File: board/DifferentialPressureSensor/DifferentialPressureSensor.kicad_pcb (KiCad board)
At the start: 2 copper layers, 119.5 x 65 mm, 15 parts, among them U1 ESP32-S3-DEVKIT-LIPO

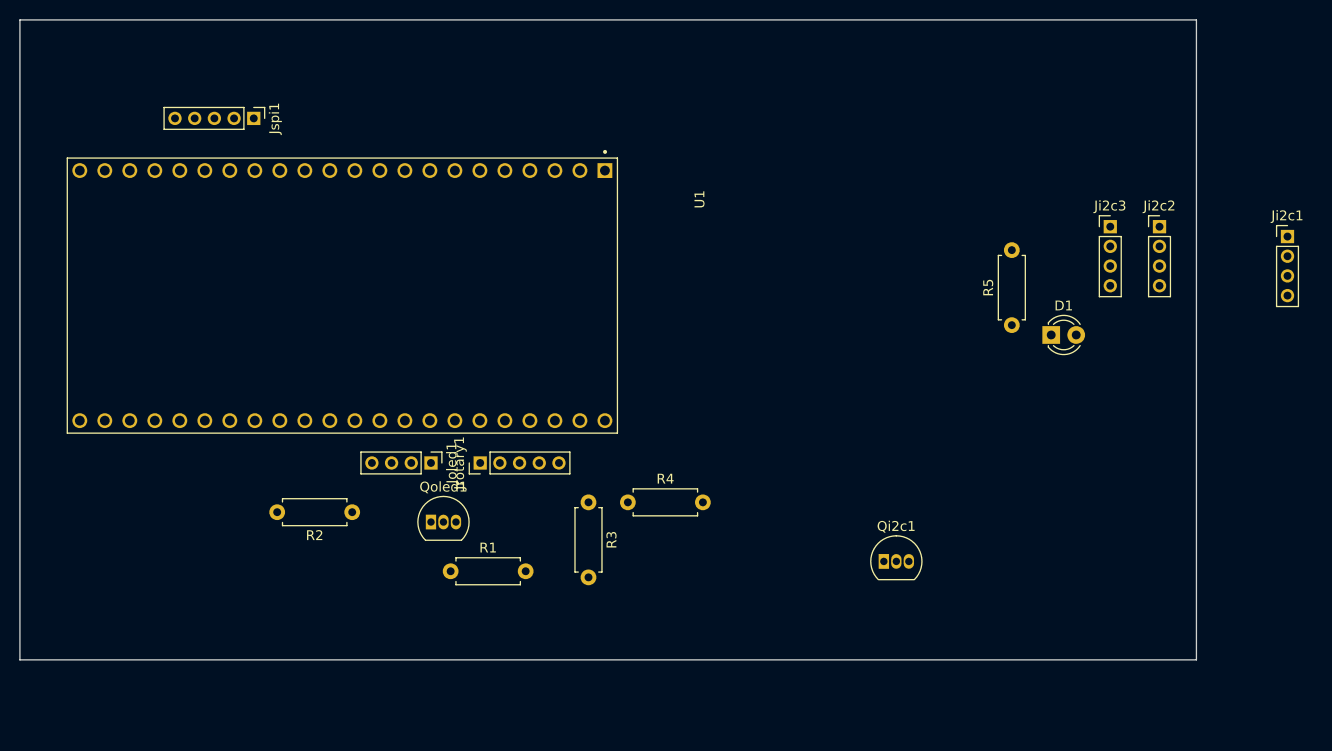
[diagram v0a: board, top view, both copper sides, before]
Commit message: updated pins on sch file and completed routing of PCB, sucks bad, but holds togeter with 1 layer only :-D
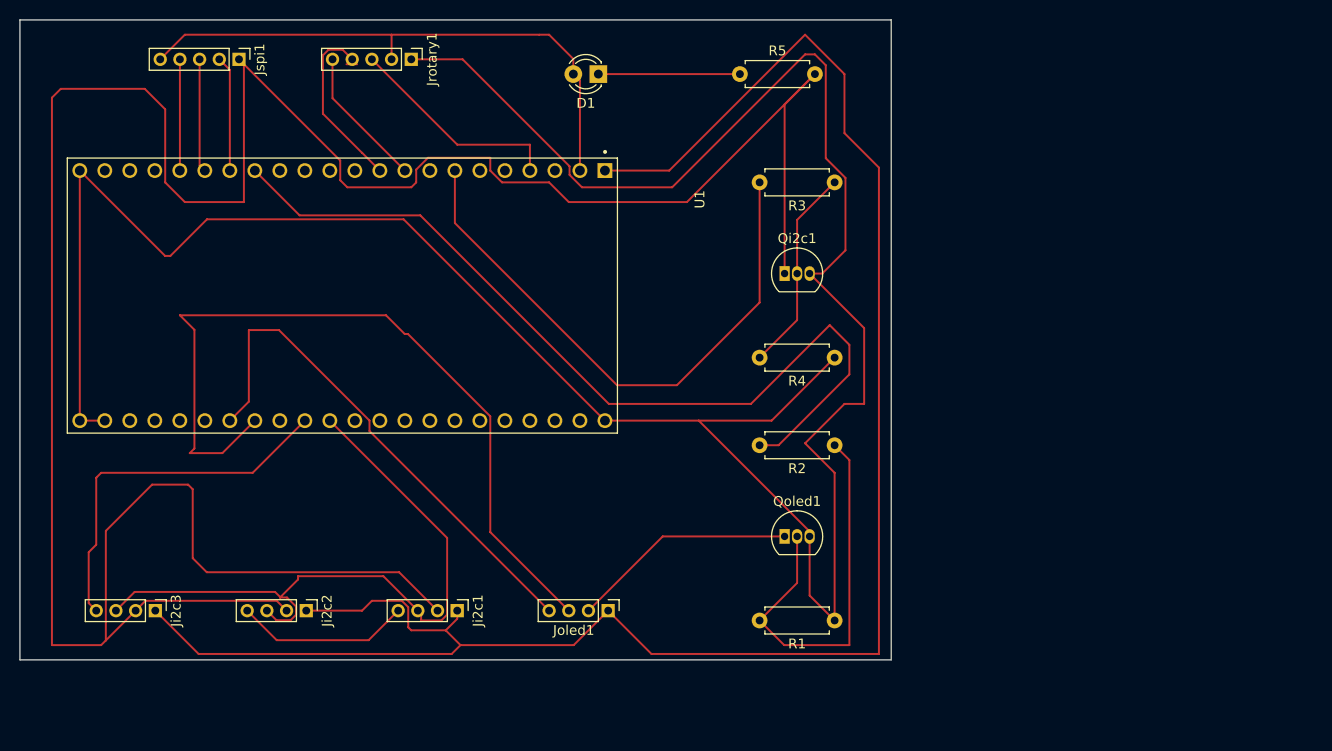
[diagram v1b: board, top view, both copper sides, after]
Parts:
- R4: value 10k -> 4.7k
- R5: value 2k -> 4.7k
- moved Ji2c3 104.5 mm to (27.0, 81.0), turned to -90 degrees
- moved Ji2c2 95.0 mm to (42.3, 81.0), turned to -90 degrees
- moved Ji2c1 92.5 mm to (57.7, 81.0), turned to -90 degrees
- moved D1 53.1 mm to (72.0, 26.5), turned to 180 degrees
- moved R2 49.5 mm to (96.0, 64.2)
- moved Jrotary1 41.6 mm to (53.0, 25.0), turned to -90 degrees
- moved R3 41.0 mm to (96.0, 37.5), turned to 180 degrees
- moved R1 39.3 mm to (96.0, 82.0), turned to 180 degrees
- moved R5 37.6 mm to (86.4, 26.5), turned to 0 degrees
- moved Qoled1 35.9 mm to (90.9, 73.5)
- moved Qi2c1 30.9 mm to (90.9, 46.8)
- moved R4 25.6 mm to (96.0, 55.3), turned to 180 degrees
- moved Joled1 23.4 mm to (73.0, 81.0)
- moved Jspi1 6.18 mm to (35.5, 25.0)
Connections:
- Ji2c1 pad 4: Net-(Ji2c1-Pin_4) -> Net-(Ji2c1-Pin_3)
- Ji2c2 pad 4: Net-(Ji2c1-Pin_4) -> Net-(Ji2c1-Pin_3)
- Ji2c3 pad 4: Net-(Ji2c1-Pin_4) -> Net-(Ji2c1-Pin_3)
- Jrotary1 pad 1: +3.3V -> GND
- Jrotary1 pad 2: GND -> +3.3V
- R2 pad 2: Net-(U1-GPIO45) -> Net-(U1-GPIO9)
- R3 pad 2: Net-(U1-U0RXD/GPIO44) -> Net-(U1-GPIO7)
- U1 pad J1_10: unconnected-(U1-GPIO17/U1TXD-PadJ1_10) -> Net-(Jrotary1-Pin_4)
- U1 pad J1_15: unconnected-(U1-GPIO9-PadJ1_15) -> Net-(U1-GPIO9)
- U1 pad J1_4: unconnected-(U1-GPIO4-PadJ1_4) -> Net-(Jrotary1-Pin_3)
- U1 pad J1_7: unconnected-(U1-GPIO7-PadJ1_7) -> Net-(U1-GPIO7)
- U1 pad J1_9: unconnected-(U1-GPIO16-PadJ1_9) -> Net-(Jrotary1-Pin_5)
- U1 pad J3_10: Net-(Ji2c1-Pin_4) -> unconnected-(U1-GPIO38/LED1-PadJ3_10)
- U1 pad J3_11: Net-(Ji2c1-Pin_3) -> unconnected-(U1-GPIO37-PadJ3_11)
- U1 pad J3_12: unconnected-(U1-GPIO36-PadJ3_12) -> Net-(Ji2c1-Pin_3)
- U1 pad J3_13: unconnected-(U1-GPIO35-PadJ3_13) -> Net-(Ji2c1-Pin_3)
- U1 pad J3_15: Net-(U1-GPIO45) -> Net-(Joled1-Pin_3)
- U1 pad J3_16: unconnected-(U1-GPIO48/I2C_SDA-PadJ3_16) -> Net-(Joled1-Pin_4)
- U1 pad J3_2: Net-(Jrotary1-Pin_3) -> unconnected-(U1-U0TXD/GPIO43-PadJ3_2)
- U1 pad J3_3: Net-(U1-U0RXD/GPIO44) -> unconnected-(U1-U0RXD/GPIO44-PadJ3_3)
- U1 pad J3_6: Net-(Jrotary1-Pin_4) -> unconnected-(U1-GPIO42-PadJ3_6)
- U1 pad J3_7: Net-(Jrotary1-Pin_5) -> unconnected-(U1-GPIO41-PadJ3_7)
- U1 pad J3_8: Net-(Joled1-Pin_4) -> unconnected-(U1-GPIO40-PadJ3_8)
- U1 pad J3_9: Net-(Joled1-Pin_3) -> unconnected-(U1-GPIO39-PadJ3_9)
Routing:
- net Net-(Ji2c1-Pin_2): track 0.00 -> 278.2 mm
- net GND: track 0.00 -> 267.6 mm
- net +3.3V: track 0.00 -> 250.8 mm
- net Net-(Ji2c1-Pin_3): track 0.00 -> 124.9 mm
- net Net-(U1-GPIO9): track 0.00 -> 89.5 mm
- net Net-(Joled1-Pin_3): track 0.00 -> 81.6 mm
- net Net-(U1-GPIO7): track 0.00 -> 58.8 mm
- net Net-(Joled1-Pin_4): track 0.00 -> 52.9 mm
- net Net-(Qoled1-G): track 0.00 -> 41.2 mm
- net Net-(Joled1-Pin_2): track 0.00 -> 23.0 mm
- net Net-(Jrotary1-Pin_3): track 0.00 -> 22.3 mm
- net Net-(Qi2c1-G): track 0.00 -> 21.0 mm
- net Net-(Jrotary1-Pin_4): track 0.00 -> 18.8 mm
- net Net-(D1-K): track 0.00 -> 14.4 mm
- net Net-(Jrotary1-Pin_5): track 0.00 -> 14.3 mm
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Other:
- board size 119.5 x 65 mm -> 88.5 x 65 mm

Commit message: fixed error on schematic, applied auto routing, created components bom
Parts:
- R1: value 10k -> 4.7k
- moved R3 3.75 mm to (94.0, 34.3)
- moved Qi2c1 3.39 mm to (88.9, 44.0)
- moved R4 3.05 mm to (94.0, 53.0)
- moved R2 2.74 mm to (94.0, 62.3)
- moved Qoled1 2.46 mm to (88.9, 72.0)
- moved R1 2.24 mm to (94.0, 81.0)
- moved R5 1.50 mm to (86.4, 25.0)
- moved D1 0.79 mm to (72.0, 25.7)
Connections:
- Ji2c1 pad 4: Net-(Ji2c1-Pin_3) -> Net-(Ji2c1-Pin_4)
- Ji2c2 pad 4: Net-(Ji2c1-Pin_3) -> Net-(Ji2c1-Pin_4)
- Ji2c3 pad 4: Net-(Ji2c1-Pin_3) -> Net-(Ji2c1-Pin_4)
- U1 pad J3_13: Net-(Ji2c1-Pin_3) -> Net-(Ji2c1-Pin_4)
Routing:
- net Net-(Ji2c1-Pin_3): track 124.9 -> 64.1 mm
- net Net-(Ji2c1-Pin_2): track 278.2 -> 225.4 mm
- net Net-(Ji2c1-Pin_4): track 0.00 -> 50.3 mm
- net +3.3V: track 250.8 -> 215.3 mm
- net Net-(Joled1-Pin_3): track 81.6 -> 50.4 mm
- net Net-(U1-GPIO9): track 89.5 -> 60.7 mm
- net Net-(U1-GPIO7): track 58.8 -> 31.4 mm
- net GND: track 267.6 -> 245.2 mm
- net Net-(Qoled1-G): track 41.2 -> 21.8 mm
- net Net-(Joled1-Pin_4): track 52.9 -> 42.1 mm
- net Net-(Jrotary1-Pin_4): track 18.8 -> 12.5 mm
- net Net-(Jrotary1-Pin_5): track 14.3 -> 17.2 mm
- net Net-(Jrotary1-Pin_3): track 22.3 -> 23.7 mm
- net Net-(Joled1-Pin_2): track 23.0 -> 21.6 mm
- net Net-(Qi2c1-G): track 21.0 -> 21.8 mm

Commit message: doc
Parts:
- moved R5 22.9 mm to (108.1, 32.2)
- moved Ji2c1 22.9 mm to (79.4, 88.2)
- moved Ji2c2 22.9 mm to (64.1, 88.2)
- moved Ji2c3 22.9 mm to (48.7, 88.2)
- moved Jspi1 22.9 mm to (57.2, 32.2)
- moved D1 22.9 mm to (93.7, 32.9)
- moved Joled1 22.9 mm to (94.7, 88.2)
- moved Jrotary1 22.9 mm to (74.7, 32.2)
- moved Qi2c1 22.9 mm to (110.7, 51.2)
- moved Qoled1 22.9 mm to (110.7, 79.2)
- moved R1 22.9 mm to (115.7, 88.2)
- moved R2 22.9 mm to (115.7, 69.5)
- moved R3 22.9 mm to (115.7, 41.5)
- moved R4 22.9 mm to (115.7, 60.2)
- moved U1 22.9 mm to (67.7, 56.2)
